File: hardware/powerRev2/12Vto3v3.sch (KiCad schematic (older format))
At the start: 10 parts

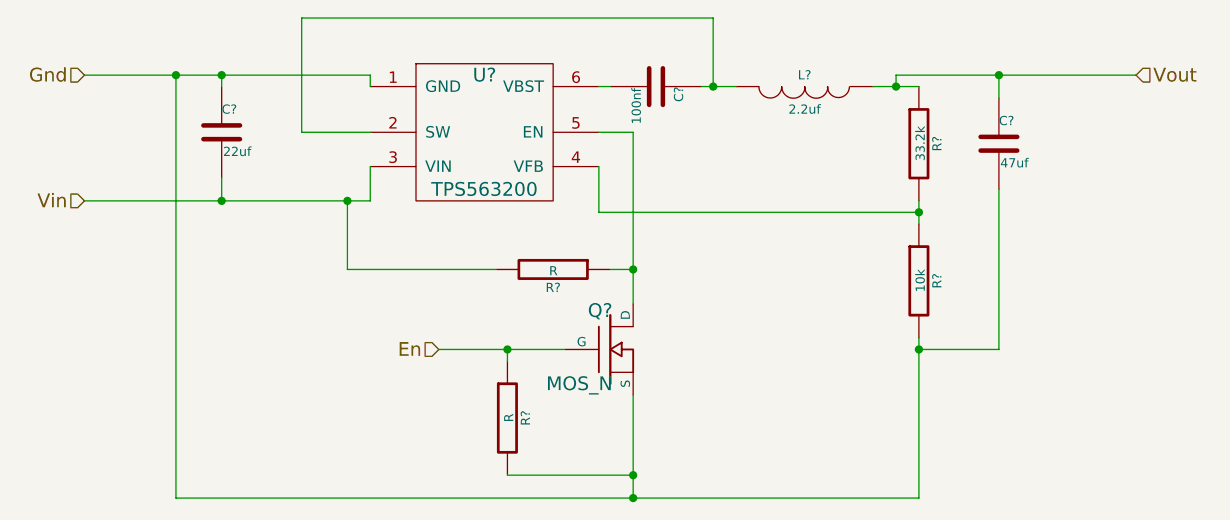
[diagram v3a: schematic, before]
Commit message: More work on the power supply
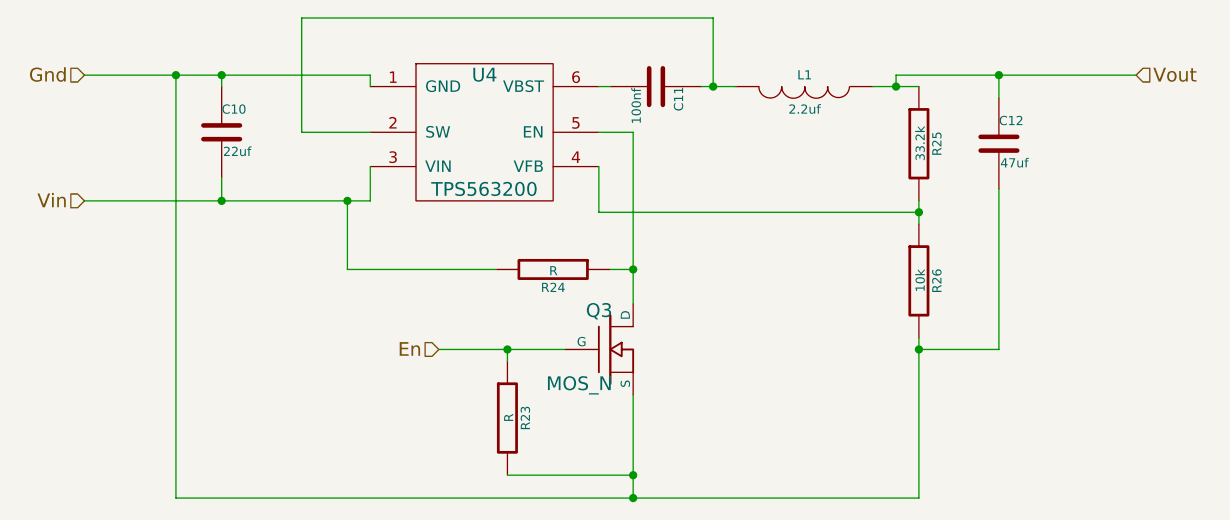
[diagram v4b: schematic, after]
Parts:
- gave numbers to parts that had none: 10
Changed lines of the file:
@@
 LIBS:KL03-QFN24
 LIBS:ncp508
+LIBS:hardwareRev1-cache
 LIBS:powerRev2-cache
 EELAYER 25 0
@@
 $EndDescr
 $Comp
-L TPS563200 U?
+L TPS563200 U4
 U 1 1 5611FCFD
 P 6000 2850
-F 0 "U?" H 6000 3400 60  0000 C CNN
+F 0 "U4" H 6000 3400 60  0000 C CNN
 F 1 "TPS563200" H 6000 2900 60  0000 C CNN
 F 2 "" H 6000 2850 60  0000 C CNN
@@
 $EndComp
 $Comp
-L C C?
+L C C10
 U 1 1 5611FD47
 P 4850 2550
-F 0 "C?" H 4850 2650 40  0000 L CNN
+F 0 "C10" H 4850 2650 40  0000 L CNN
 F 1 "22uf" H 4856 2465 40  0000 L CNN
 F 2 "" H 4888 2400 30  0000 C CNN
@@
 Connection ~ 4850 2850
 $Comp
-L C C?
+L C C11
 U 1 1 5611FDFD
 P 6750 2350
-F 0 "C?" H 6750 2450 40  0000 L CNN
+F 0 "C11" H 6750 2450 40  0000 L CNN
 F 1 "100nf" H 6756 2265 40  0000 L CNN
 F 2 "" H 6788 2200 30  0000 C CNN
@@
 $EndComp
 $Comp
-L R R?
+L R R25
 U 1 1 5611FE98
 P 7900 2600
-F 0 "R?" V 7980 2600 40  0000 C CNN
+F 0 "R25" V 7980 2600 40  0000 C CNN
 F 1 "33.2k" V 7907 2601 40  0000 C CNN
 F 2 "" V 7830 2600 30  0000 C CNN
@@
 $EndComp
 $Comp
-L R R?
+L R R26
 U 1 1 5611FECF
 P 7900 3200
-F 0 "R?" V 7980 3200 40  0000 C CNN
+F 0 "R26" V 7980 3200 40  0000 C CNN
 F 1 "10k" V 7907 3201 40  0000 C CNN
 F 2 "" V 7830 3200 30  0000 C CNN
@@
 $EndComp
 $Comp
-L INDUCTOR L?
+L INDUCTOR L1
 U 1 1 5611FEEF
 P 7400 2350
-F 0 "L?" V 7350 2350 40  0000 C CNN
+F 0 "L1" V 7350 2350 40  0000 C CNN
 F 1 "2.2uf" V 7500 2350 40  0000 C CNN
 F 2 "" H 7400 2350 60  0000 C CNN
@@
 	6650 2550 6650 3300
 $Comp
-L R R?
+L R R24
 U 1 1 56120123
 P 6300 3150
-F 0 "R?" V 6380 3150 40  0000 C CNN
+F 0 "R24" V 6380 3150 40  0000 C CNN
 F 1 "R" V 6307 3151 40  0000 C CNN
 F 2 "" V 6230 3150 30  0000 C CNN
@@
 	6650 3700 6650 4150
 $Comp
-L MOS_N Q?
+L MOS_N Q3
 U 1 1 561201E9
 P 6550 3500
-F 0 "Q?" H 6560 3670 60  0000 R CNN
+F 0 "Q3" H 6560 3670 60  0000 R CNN
 F 1 "MOS_N" H 6560 3350 60  0000 R CNN
 F 2 "" H 6550 3500 60  0000 C CNN
@@
 $EndComp
 $Comp
-L R R?
+L R R23
 U 1 1 561202C6
 P 6100 3800
-F 0 "R?" V 6180 3800 40  0000 C CNN
+F 0 "R23" V 6180 3800 40  0000 C CNN
 F 1 "R" V 6107 3801 40  0000 C CNN
 F 2 "" V 6030 3800 30  0000 C CNN
@@
 En
 $Comp
-L C C?
+L C C12
 U 1 1 561203D3
 P 8250 2600
-F 0 "C?" H 8250 2700 40  0000 L CNN
+F 0 "C12" H 8250 2700 40  0000 L CNN
 F 1 "47uf" H 8256 2515 40  0000 L CNN
 F 2 "" H 8288 2450 30  0000 C CNN

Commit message: Started the new power board PCB. Made it pretty far.
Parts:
- C10: footprint (none) -> Capacitors_SMD:C_1206; Manufacturer PN (none) -> GRM31CR61E226ME15L
- C11: footprint (none) -> Capacitors_SMD:C_0402
- C12: footprint (none) -> Capacitors_SMD:C_1206; Manufacturer PN (none) -> GRM31CE70J476ME15L
- L1: value 2.2uf -> 2.2uh; footprint (none) -> SMD_Packages:SMD-2010_Pol; Manufacturer PN (none) -> TYS50402R2N-10
- Q3: footprint (none) -> Housings_SOT-23_SOT-143_TSOT-6:SOT-23; Manufacturer PN (none) -> 2N7002P,215
- R23, R25, R26: footprint (none) -> Resistors_SMD:R_0402
- R24: value R -> 10K; footprint (none) -> Resistors_SMD:R_0402
- U5: renamed from U4; footprint (none) -> Housings_SOT-23_SOT-143_TSOT-6:SOT-23-6
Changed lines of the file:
@@
 LIBS:ncp508
 LIBS:hardwareRev1-cache
+LIBS:Tag-Connect
+LIBS:mpcie
+LIBS:RF-Head2
+LIBS:ritli-rfhead
 LIBS:powerRev2-cache
 EELAYER 25 0
@@
 $EndDescr
 $Comp
-L TPS563200 U4
+L TPS563200 U5
 U 1 1 5611FCFD
 P 6000 2850
-F 0 "U4" H 6000 3400 60  0000 C CNN
+F 0 "U5" H 6000 3400 60  0000 C CNN
 F 1 "TPS563200" H 6000 2900 60  0000 C CNN
-F 2 "" H 6000 2850 60  0000 C CNN
+F 2 "Housings_SOT-23_SOT-143_TSOT-6:SOT-23-6" H 6000 2850 60  0001 C CNN
 F 3 "" H 6000 2850 60  0000 C CNN
 	1    6000 2850
@@
 F 0 "C10" H 4850 2650 40  0000 L CNN
 F 1 "22uf" H 4856 2465 40  0000 L CNN
-F 2 "" H 4888 2400 30  0000 C CNN
+F 2 "Capacitors_SMD:C_1206" H 4888 2400 30  0001 C CNN
 F 3 "" H 4850 2550 60  0000 C CNN
+F 4 "GRM31CR61E226ME15L" H 4850 2550 60  0001 C CNN "Manufacturer PN"
 	1    4850 2550
 	1    0    0    -1
@@
 F 0 "C11" H 6750 2450 40  0000 L CNN
 F 1 "100nf" H 6756 2265 40  0000 L CNN
-F 2 "" H 6788 2200 30  0000 C CNN
+F 2 "Capacitors_SMD:C_0402" H 6788 2200 30  0001 C CNN
 F 3 "" H 6750 2350 60  0000 C CNN
 	1    6750 2350
@@
 F 0 "R25" V 7980 2600 40  0000 C CNN
 F 1 "33.2k" V 7907 2601 40  0000 C CNN
-F 2 "" V 7830 2600 30  0000 C CNN
+F 2 "Resistors_SMD:R_0402" V 7830 2600 30  0001 C CNN
 F 3 "" H 7900 2600 30  0000 C CNN
 	1    7900 2600
@@
 F 0 "R26" V 7980 3200 40  0000 C CNN
 F 1 "10k" V 7907 3201 40  0000 C CNN
-F 2 "" V 7830 3200 30  0000 C CNN
+F 2 "Resistors_SMD:R_0402" V 7830 3200 30  0001 C CNN
 F 3 "" H 7900 3200 30  0000 C CNN
 	1    7900 3200
@@
 P 7400 2350
 F 0 "L1" V 7350 2350 40  0000 C CNN
-F 1 "2.2uf" V 7500 2350 40  0000 C CNN
-F 2 "" H 7400 2350 60  0000 C CNN
+F 1 "2.2uh" V 7500 2350 40  0000 C CNN
+F 2 "SMD_Packages:SMD-2010_Pol" H 7400 2350 60  0001 C CNN
 F 3 "" H 7400 2350 60  0000 C CNN
+F 4 "TYS50402R2N-10" H 7400 2350 60  0001 C CNN "Manufacturer PN"
 	1    7400 2350
 	0    1    1    0
@@
 P 6300 3150
 F 0 "R24" V 6380 3150 40  0000 C CNN
-F 1 "R" V 6307 3151 40  0000 C CNN
-F 2 "" V 6230 3150 30  0000 C CNN
+F 1 "10K" V 6307 3151 40  0000 C CNN
+F 2 "Resistors_SMD:R_0402" V 6230 3150 30  0001 C CNN
 F 3 "" H 6300 3150 30  0000 C CNN
 	1    6300 3150
@@
 F 0 "Q3" H 6560 3670 60  0000 R CNN
 F 1 "MOS_N" H 6560 3350 60  0000 R CNN
-F 2 "" H 6550 3500 60  0000 C CNN
+F 2 "Housings_SOT-23_SOT-143_TSOT-6:SOT-23" H 6550 3500 60  0001 C CNN
 F 3 "" H 6550 3500 60  0000 C CNN
+F 4 "2N7002P,215" H 6550 3500 60  0001 C CNN "Manufacturer PN"
 	1    6550 3500
 	1    0    0    -1
@@
 F 0 "R23" V 6180 3800 40  0000 C CNN
 F 1 "R" V 6107 3801 40  0000 C CNN
-F 2 "" V 6030 3800 30  0000 C CNN
+F 2 "Resistors_SMD:R_0402" V 6030 3800 30  0001 C CNN
 F 3 "" H 6100 3800 30  0000 C CNN
 	1    6100 3800
@@
 F 0 "C12" H 8250 2700 40  0000 L CNN
 F 1 "47uf" H 8256 2515 40  0000 L CNN
-F 2 "" H 8288 2450 30  0000 C CNN
+F 2 "Capacitors_SMD:C_1206" H 8288 2450 30  0001 C CNN
 F 3 "" H 8250 2600 60  0000 C CNN
+F 4 "GRM31CE70J476ME15L" H 8250 2600 60  0001 C CNN "Manufacturer PN"
 	1    8250 2600
 	1    0    0    -1

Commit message: Finished the new power board.
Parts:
- removed Q3: MOS_N, Housings_SOT-23_SOT-143_TSOT-6:SOT-23, symbol MOS_N
- added Q3: MOS_N_numbered, Housings_SOT-23_SOT-143_TSOT-6:SOT-23, symbol MOS_N_numbered
- R23: value R -> 10K
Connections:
- net En: now also Q3.1 (G)
- net Gnd: now also Q3.2 (S)
- net at R24.1, U5.5 (EN): now also Q3.3 (D)
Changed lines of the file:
@@
 EESchema Schematic File Version 2
+LIBS:powerRev2-rescue
 LIBS:power
 LIBS:device
@@
 LIBS:RF-Head2
 LIBS:ritli-rfhead
+LIBS:mos_n_numbered
+LIBS:npn-numbered
 LIBS:powerRev2-cache
 EELAYER 25 0
@@
 	6650 3700 6650 4150
 $Comp
-L MOS_N Q3
-U 1 1 561201E9
-P 6550 3500
-F 0 "Q3" H 6560 3670 60  0000 R CNN
-F 1 "MOS_N" H 6560 3350 60  0000 R CNN
-F 2 "Housings_SOT-23_SOT-143_TSOT-6:SOT-23" H 6550 3500 60  0001 C CNN
-F 3 "" H 6550 3500 60  0000 C CNN
-F 4 "2N7002P,215" H 6550 3500 60  0001 C CNN "Manufacturer PN"
-	1    6550 3500
-	1    0    0    -1
-$EndComp
-$Comp
 L R R23
 U 1 1 561202C6
 P 6100 3800
 F 0 "R23" V 6180 3800 40  0000 C CNN
-F 1 "R" V 6107 3801 40  0000 C CNN
+F 1 "10K" V 6107 3801 40  0000 C CNN
 F 2 "Resistors_SMD:R_0402" V 6030 3800 30  0001 C CNN
 F 3 "" H 6100 3800 30  0000 C CNN
@@
 Connection ~ 4650 2300
 Connection ~ 6650 4150
+$Comp
+L MOS_N_numbered Q3
+U 1 1 562FE111
+P 6550 3500
+F 0 "Q3" H 6560 3670 60  0000 R CNN
+F 1 "MOS_N_numbered" H 6560 3350 60  0000 R CNN
+F 2 "Housings_SOT-23_SOT-143_TSOT-6:SOT-23" H 6550 3500 60  0001 C CNN
+F 3 "" H 6550 3500 60  0000 C CNN
+F 4 "DMG2302U" H 6550 3500 60  0001 C CNN "Manufacturer PN"
+	1    6550 3500
+	1    0    0    -1
+$EndComp
 $EndSCHEMATC
